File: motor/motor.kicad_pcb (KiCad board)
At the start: 2 copper layers, 45.5 x 34.3 mm, 13 parts, among them J1 power, J2 from switches, J3 motor, J4 towards uC, U1 L293D

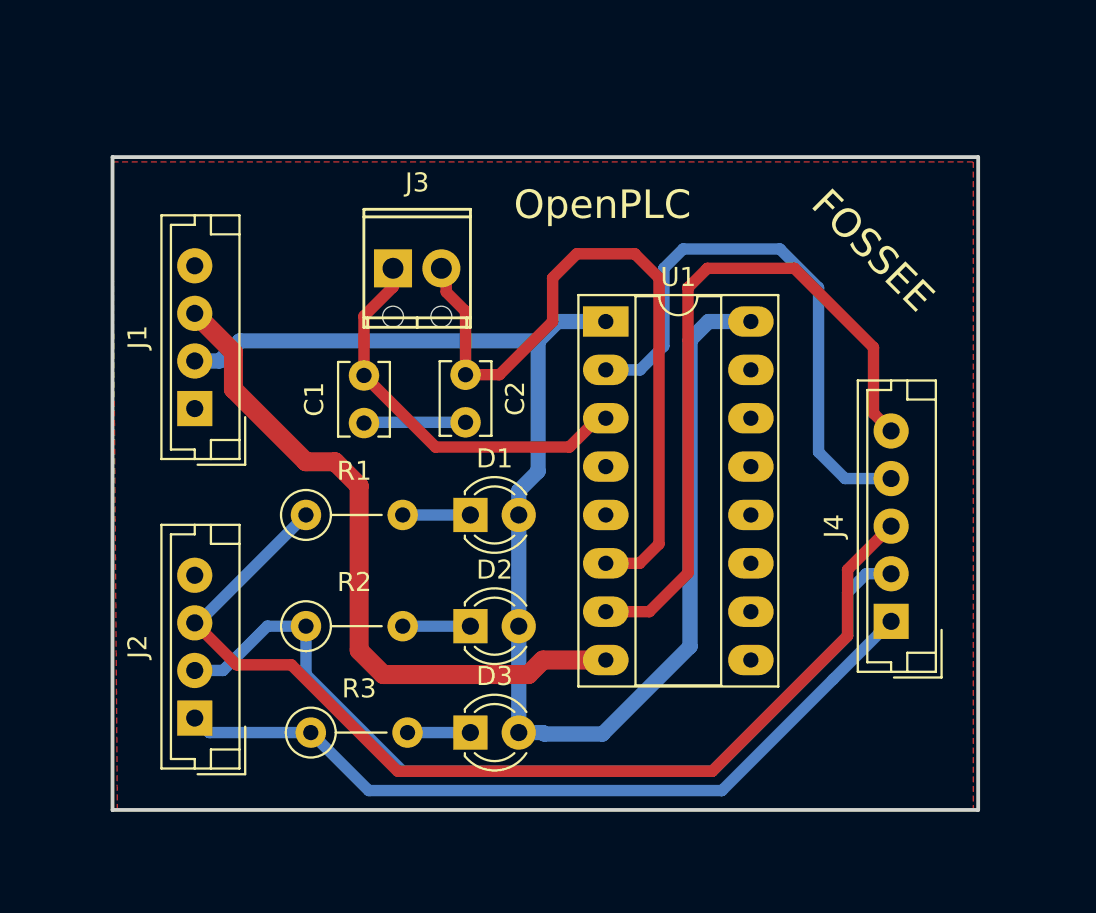
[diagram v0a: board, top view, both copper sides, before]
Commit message: changed LEds from 3mm to 5mm;added Status LED to motor-module
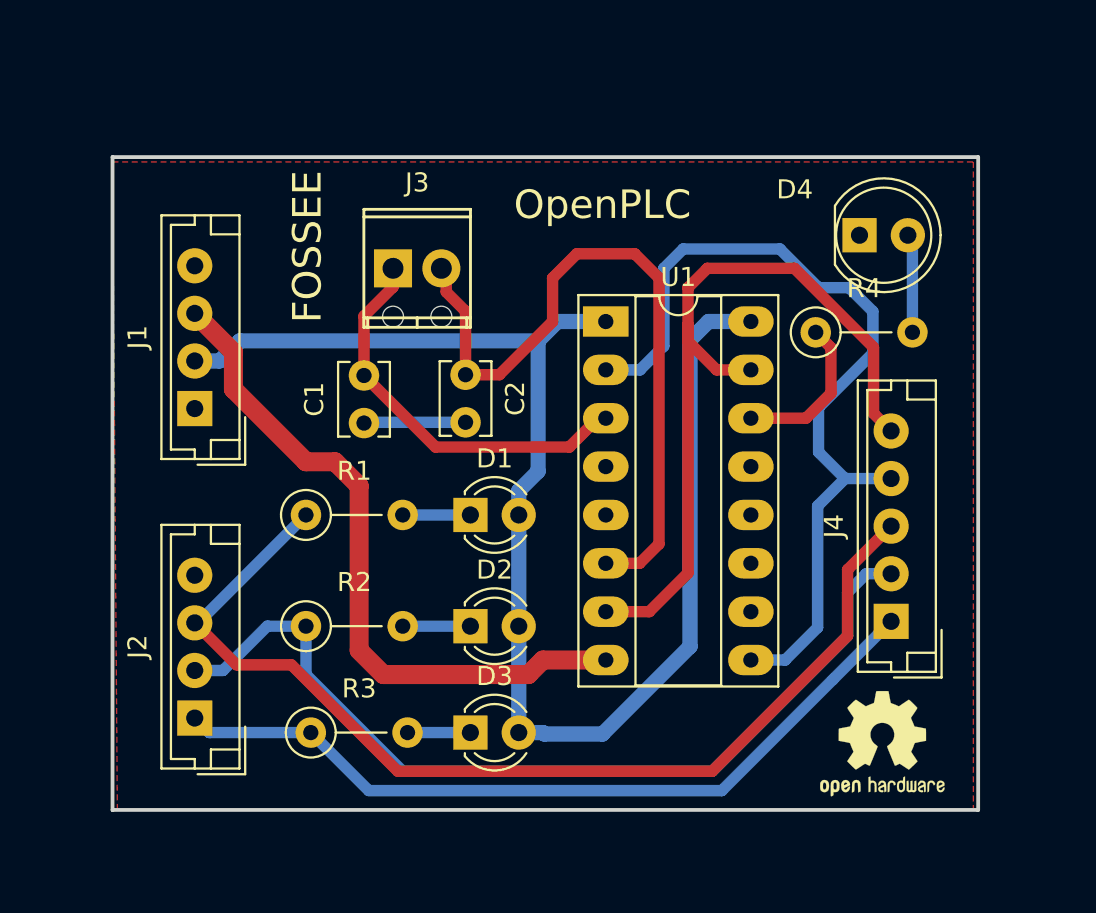
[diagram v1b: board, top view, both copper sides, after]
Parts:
- added D4: LED, LEDs:LED_D5.0mm, F.Cu at (122.8, 86.4)
- added R4: 1K, Resistors_THT:R_Axial_DIN0207_L6.3mm_D2.5mm_P5.08mm_Vertical, F.Cu at (120.5, 91.5)
- added REF***: OSHW-Logo2_7.3x6mm_SilkScreen, Symbols:OSHW-Logo2_7.3x6mm_SilkScreen, F.Cu at (124.0, 113.1)
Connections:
- U1 pad 15: Net-(U1-Pad15) -> /2a
- U1 pad 9: Net-(U1-Pad9) -> /1a
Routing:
- net /1a: track 30.1 -> 46.0 mm
- net Net-(R4-Pad1): track 0.00 -> 8.28 mm
- net Net-(D4-Pad2): track 0.00 -> 5.20 mm
- net /2a: track 36.8 -> 41.6 mm

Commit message: added indicator LED's in heater module; added proper markings in motor module.
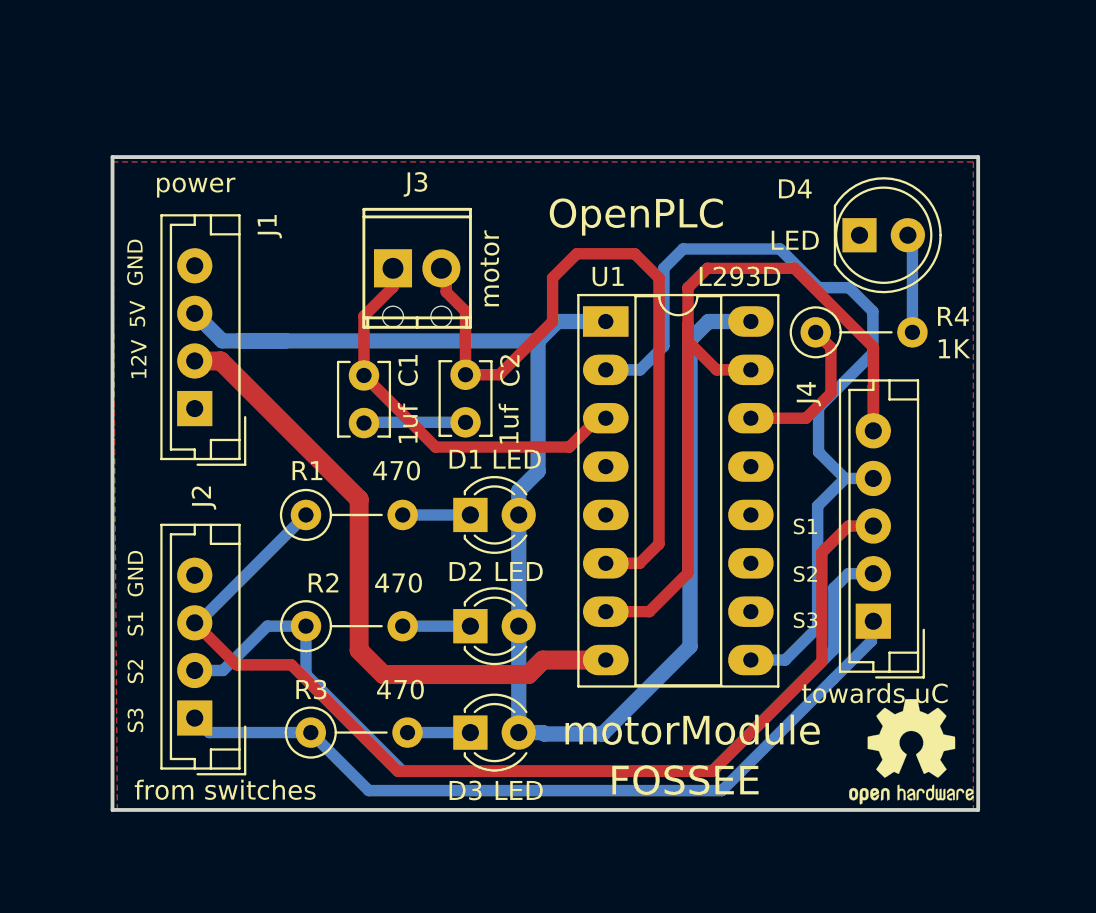
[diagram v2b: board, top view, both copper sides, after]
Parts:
- moved REF*** 1.58 mm to (125.5, 113.5)
- moved J4 0.94 mm to (123.5, 106.7)
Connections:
- J1 pad 1: GND -> Net-(J1-Pad1)
- J1 pad 2: +5V -> +12V
- J1 pad 3: +12V -> +5V
- J1 pad 4: Net-(J1-Pad4) -> GND
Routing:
- net +12V: track 36.0 -> 33.4 mm
- net +5V: track 74.1 -> 76.7 mm
- net /2a: track 41.6 -> 42.6 mm
- net /1a: track 46.0 -> 45.1 mm
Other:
- board text added: "12V"
- board text added: "5V"
- board text added: "GND"
- board text added: "S1"
- board text added: "S2"
- board text added: "S3"
- board text added: "motorModule"

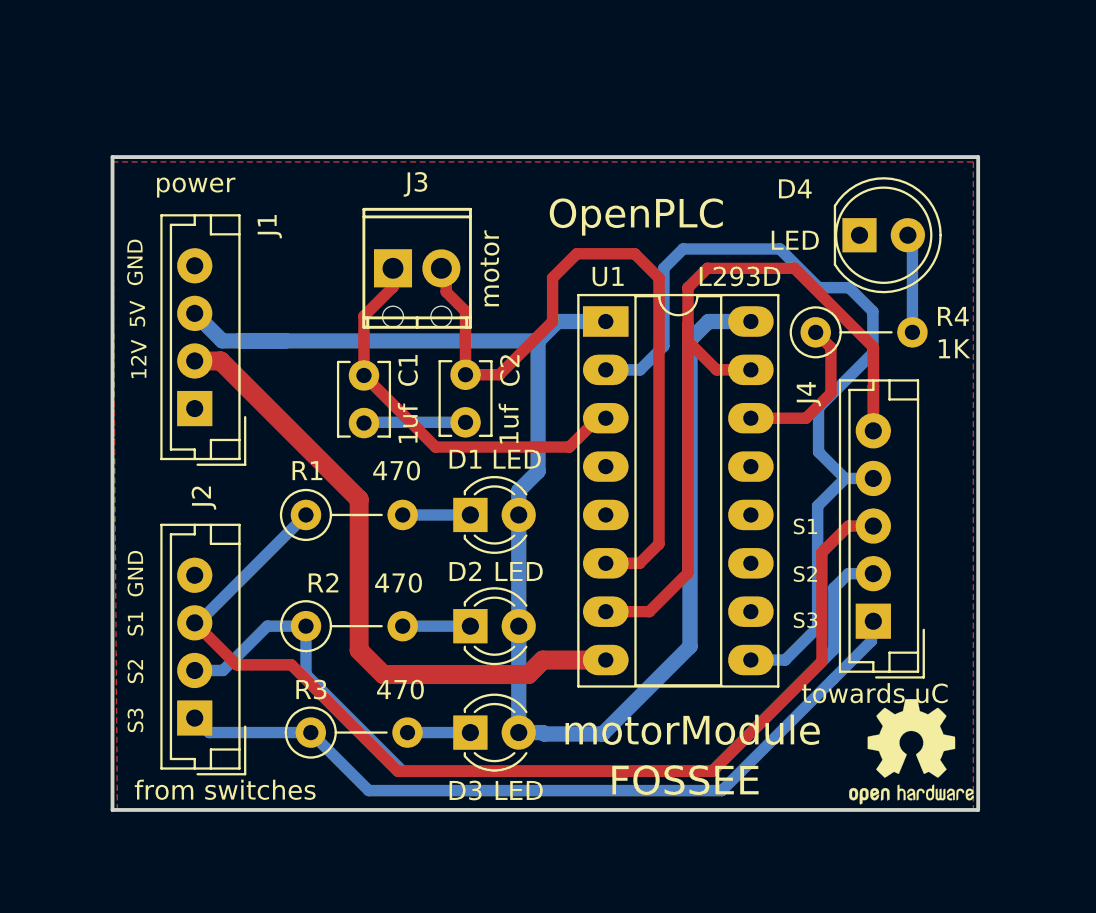
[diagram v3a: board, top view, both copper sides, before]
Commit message: mounting holes in motor, extra pins in traffic, corrections in labels
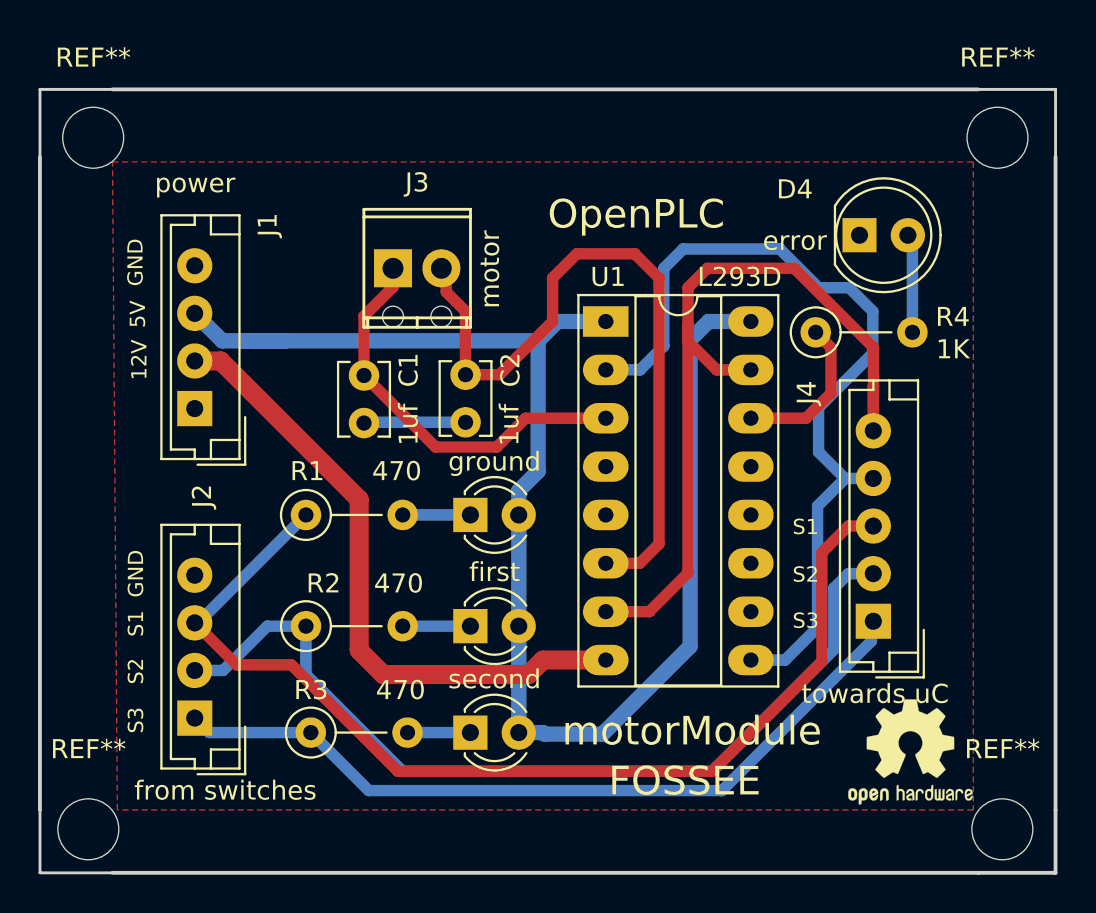
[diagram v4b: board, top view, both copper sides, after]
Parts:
- added REF**: MountingHole_3.2mm_M3, Mounting_Holes:MountingHole_3.2mm_M3, F.Cu at (82.3, 117.6)
- added REF**: MountingHole_3.2mm_M3, Mounting_Holes:MountingHole_3.2mm_M3, F.Cu at (130.3, 117.6)
- added REF**: MountingHole_3.2mm_M3, Mounting_Holes:MountingHole_3.2mm_M3, F.Cu at (82.5, 81.3)
- added REF**: MountingHole_3.2mm_M3, Mounting_Holes:MountingHole_3.2mm_M3, F.Cu at (130.0, 81.3)
- D1: value LED -> ground
- D2: value LED -> first
- D3: value LED -> second
- D4: value LED -> error
- moved REF*** 0.05 mm to (125.5, 113.5)
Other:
- board size 45.5 x 34.3 mm -> 53.3 x 41.1 mm

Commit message: corrected the mounting-scre-hole sizes to 3mm dia. drew symmetrical cutline for motor. updated README with new board images.
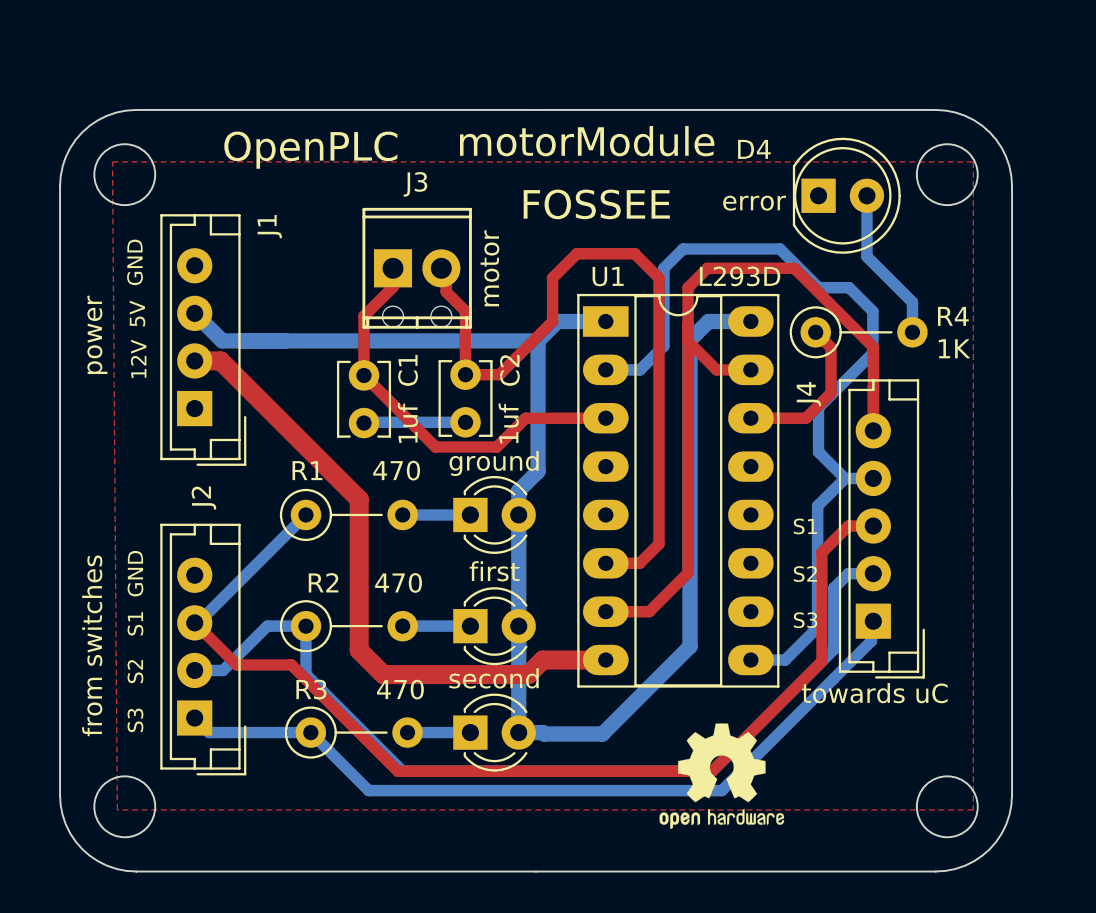
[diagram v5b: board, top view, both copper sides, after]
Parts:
- removed REF** (x4): MountingHole_3.2mm_M3, Mounting_Holes:MountingHole_3.2mm_M3
- moved REF*** 9.99 mm to (115.6, 114.8)
- moved D4 2.99 mm to (120.7, 84.3)
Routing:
- net Net-(D4-Pad2): track 5.20 -> 8.16 mm
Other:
- board size 53.3 x 41.1 mm -> 50 x 40 mm

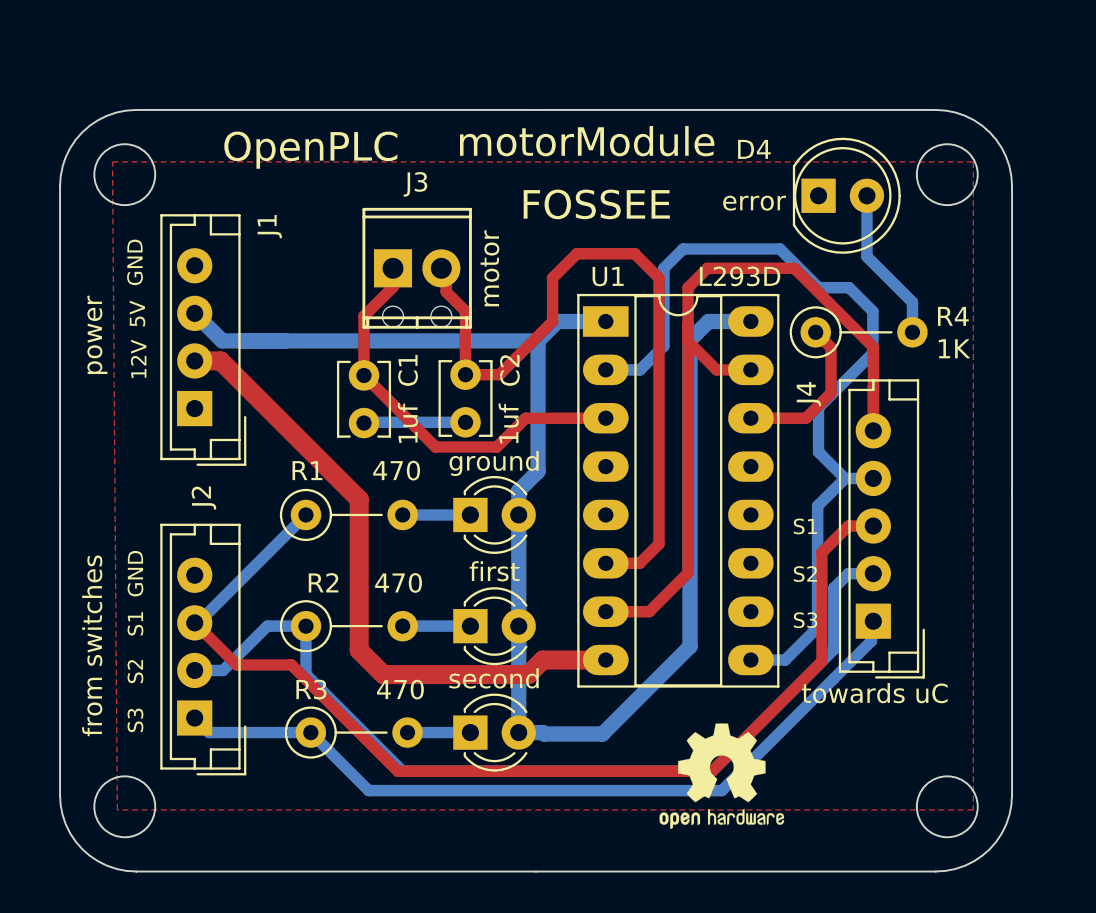
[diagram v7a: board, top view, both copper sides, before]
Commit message: swapped power and switch connector postions
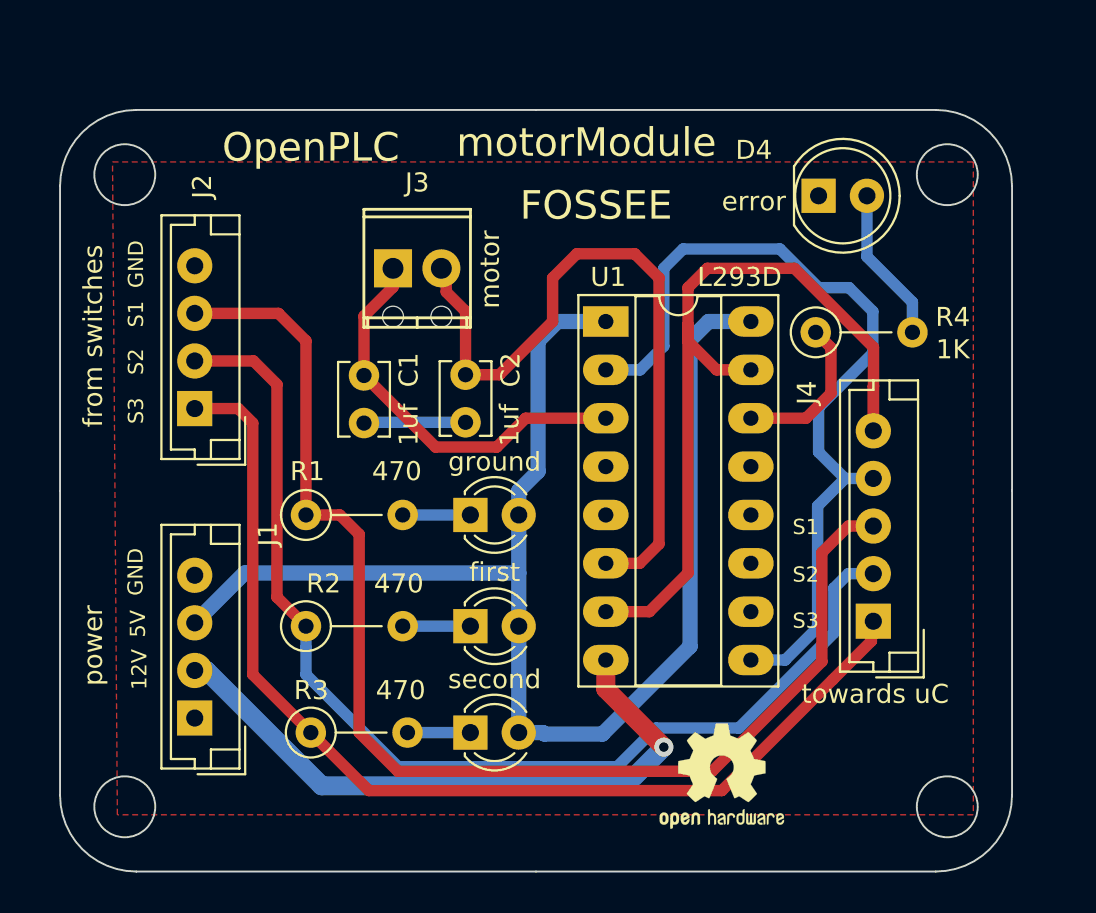
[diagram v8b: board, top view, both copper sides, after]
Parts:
- moved J1 16.3 mm to (87.9, 111.8)
- moved J2 16.3 mm to (87.9, 95.5)
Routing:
- net /sw3: track 41.5 -> 55.9 mm
- net /sw2: track 47.4 -> 58.1 mm
- net /sw1: track 55.7 -> 65.7 mm
- net +5V: track 76.7 -> 73.9 mm
- net +12V: track 33.4 -> 33.8 mm, vias 0 -> 1
